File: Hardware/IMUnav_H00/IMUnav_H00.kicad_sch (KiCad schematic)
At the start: 13 parts, among them U11 OLED_I2C, U7 STM32G474VETx

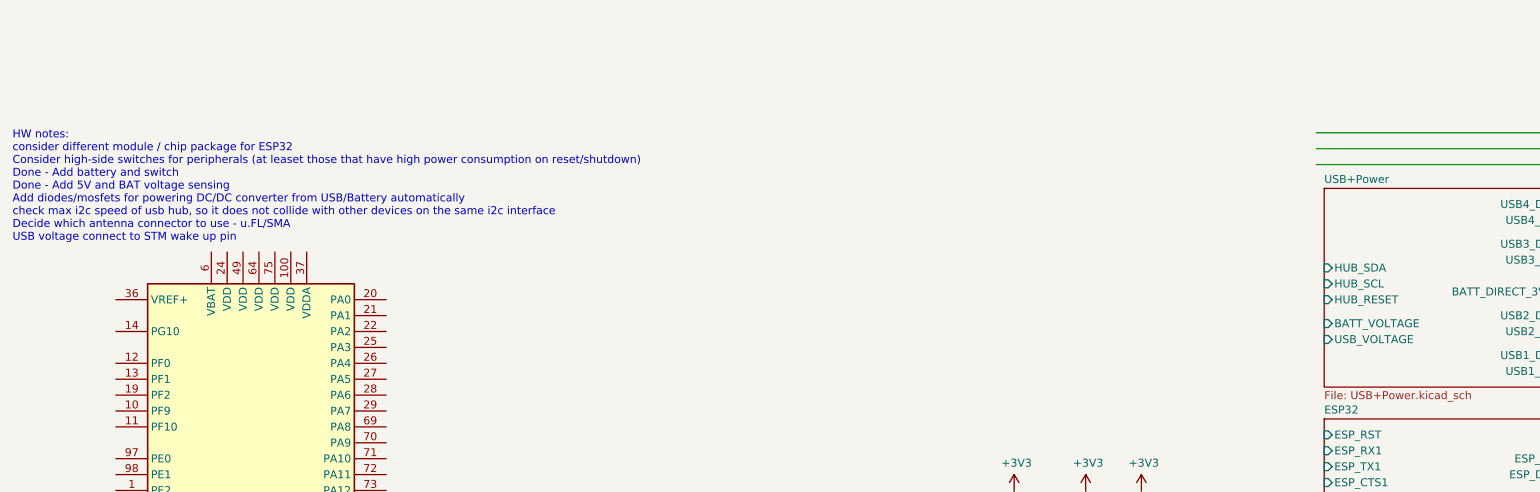
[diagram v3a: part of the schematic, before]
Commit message: Changes in power management
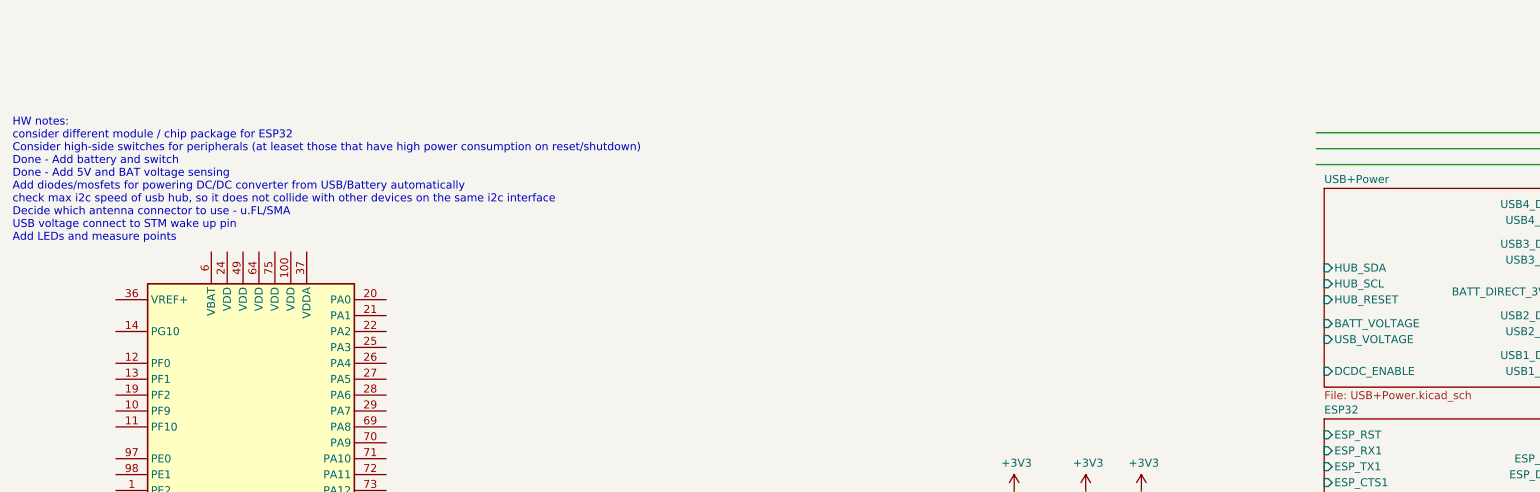
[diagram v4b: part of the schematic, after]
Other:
- sheet USB+Power ports: added DCDC_ENABLE; removed none
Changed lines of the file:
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@@
     (stroke (width 0) (type default))
   )
-  (text "HW notes:\nconsider different module / chip package for ESP32\nConsider high-side switches for peripherals (at leaset those that have high power consumption on reset/shutdown)\nDone - Add battery and switch\nDone - Add 5V and BAT voltage sensing\nAdd diodes/mosfets for powering DC/DC converter from USB/Battery automatically\ncheck max i2c speed of usb hub, so it does not collide with other devices on the same i2c interface\nDecide which antenna connector to use - u.FL/SMA\nUSB voltage connect to STM wake up pin\n\n\n"
+  (text "HW notes:\nconsider different module / chip package for ESP32\nConsider high-side switches for peripherals (at leaset those that have high power consumption on reset/shutdown)\nDone - Add battery and switch\nDone - Add 5V and BAT voltage sensing\nAdd diodes/mosfets for powering DC/DC converter from USB/Battery automatically\ncheck max i2c speed of usb hub, so it does not collide with other devices on the same i2c interface\nDecide which antenna connector to use - u.FL/SMA\nUSB voltage connect to STM wake up pin\nAdd LEDs and measure points\n\n\n"
     (at 15.24 34.29 0)
     (effects (font (size 1.27 1.27)) (justify left bottom))
@@
       (effects (font (size 1.27 1.27)) (justify right))
     )
-    (instances
+    (pin "DCDC_ENABLE" input (at 224.79 50.8 180)
+      (effects (font (size 1.27 1.27)) (justify left))
+    )
+    (instances

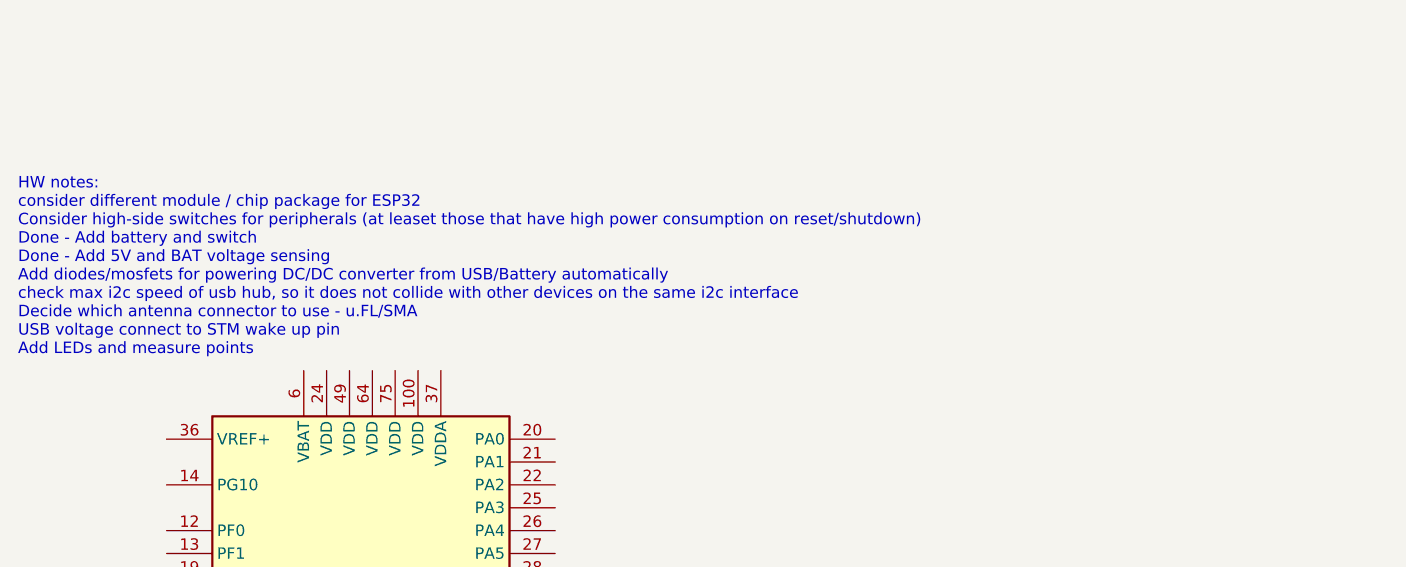
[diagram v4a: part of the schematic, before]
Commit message: Added .gitignore for KiCad file structure
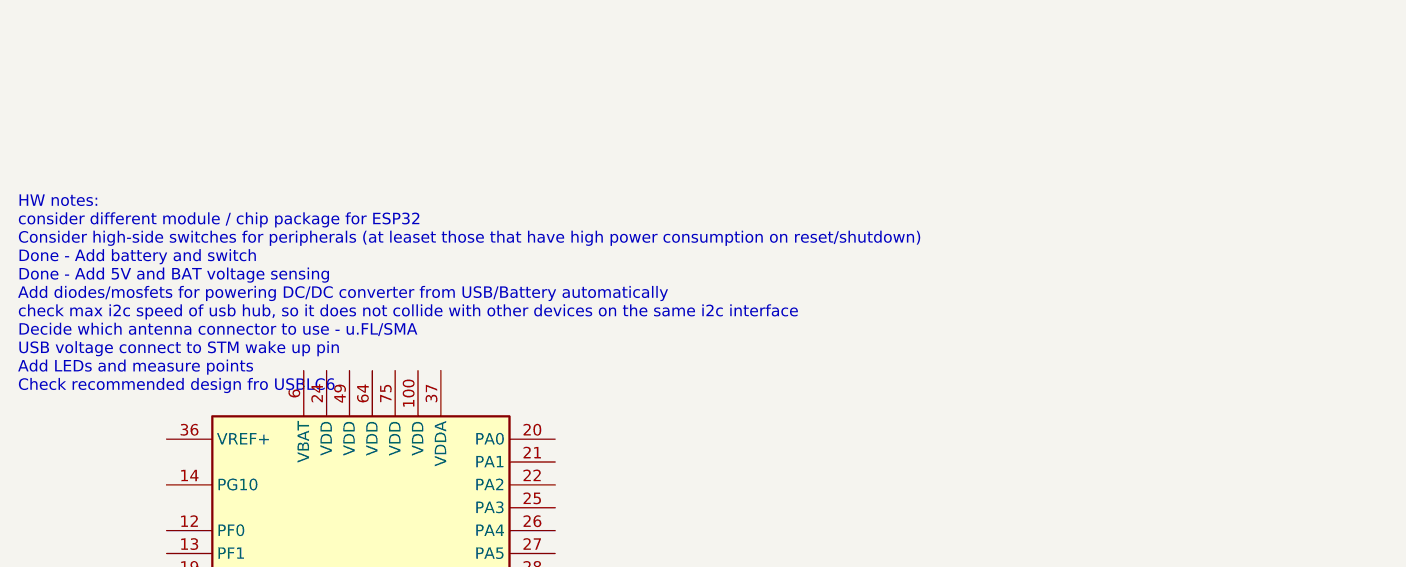
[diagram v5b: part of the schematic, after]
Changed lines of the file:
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@@
     (stroke (width 0) (type default))
   )
-  (text "HW notes:\nconsider different module / chip package for ESP32\nConsider high-side switches for peripherals (at leaset those that have high power consumption on reset/shutdown)\nDone - Add battery and switch\nDone - Add 5V and BAT voltage sensing\nAdd diodes/mosfets for powering DC/DC converter from USB/Battery automatically\ncheck max i2c speed of usb hub, so it does not collide with other devices on the same i2c interface\nDecide which antenna connector to use - u.FL/SMA\nUSB voltage connect to STM wake up pin\nAdd LEDs and measure points\n\n\n"
+  (text "HW notes:\nconsider different module / chip package for ESP32\nConsider high-side switches for peripherals (at leaset those that have high power consumption on reset/shutdown)\nDone - Add battery and switch\nDone - Add 5V and BAT voltage sensing\nAdd diodes/mosfets for powering DC/DC converter from USB/Battery automatically\ncheck max i2c speed of usb hub, so it does not collide with other devices on the same i2c interface\nDecide which antenna connector to use - u.FL/SMA\nUSB voltage connect to STM wake up pin\nAdd LEDs and measure points\nCheck recommended design fro USBLC6\n"
     (at 15.24 34.29 0)
     (effects (font (size 1.27 1.27)) (justify left bottom))

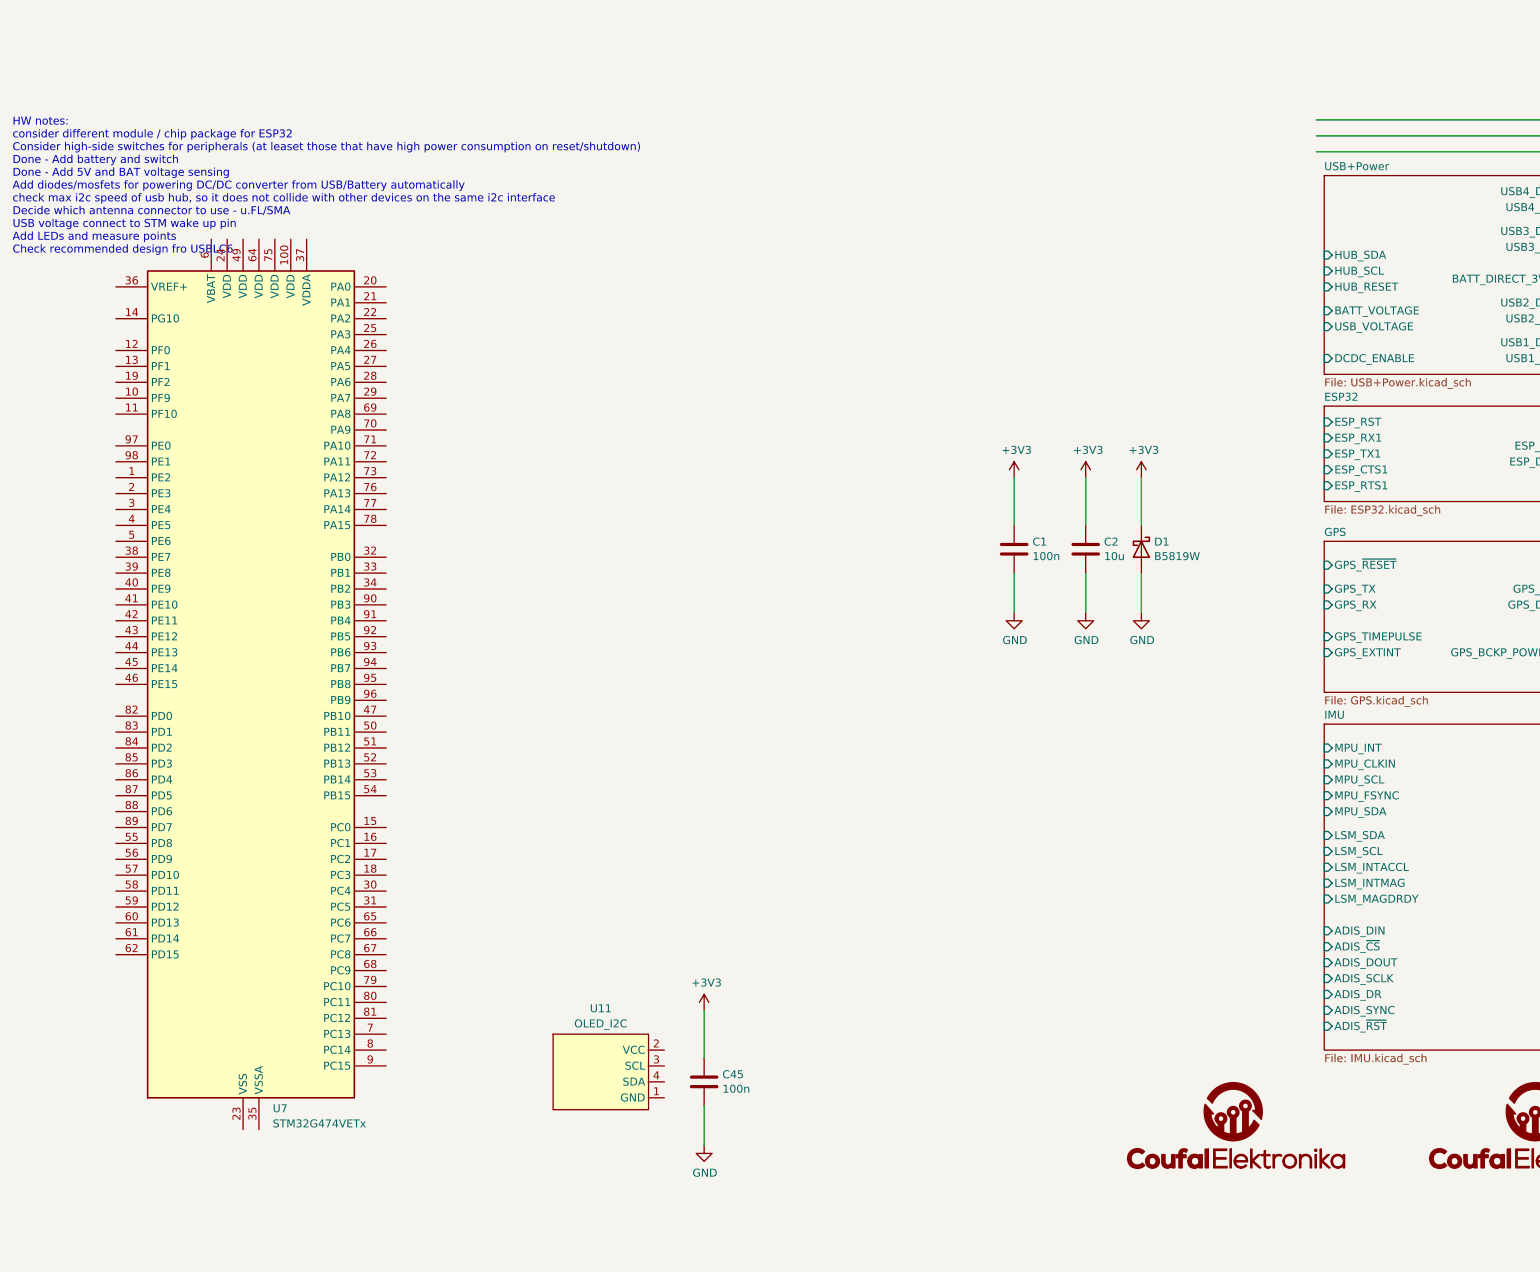
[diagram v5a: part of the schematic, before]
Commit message: Finalized and cleaned Power Management, added GPS antenna footprint
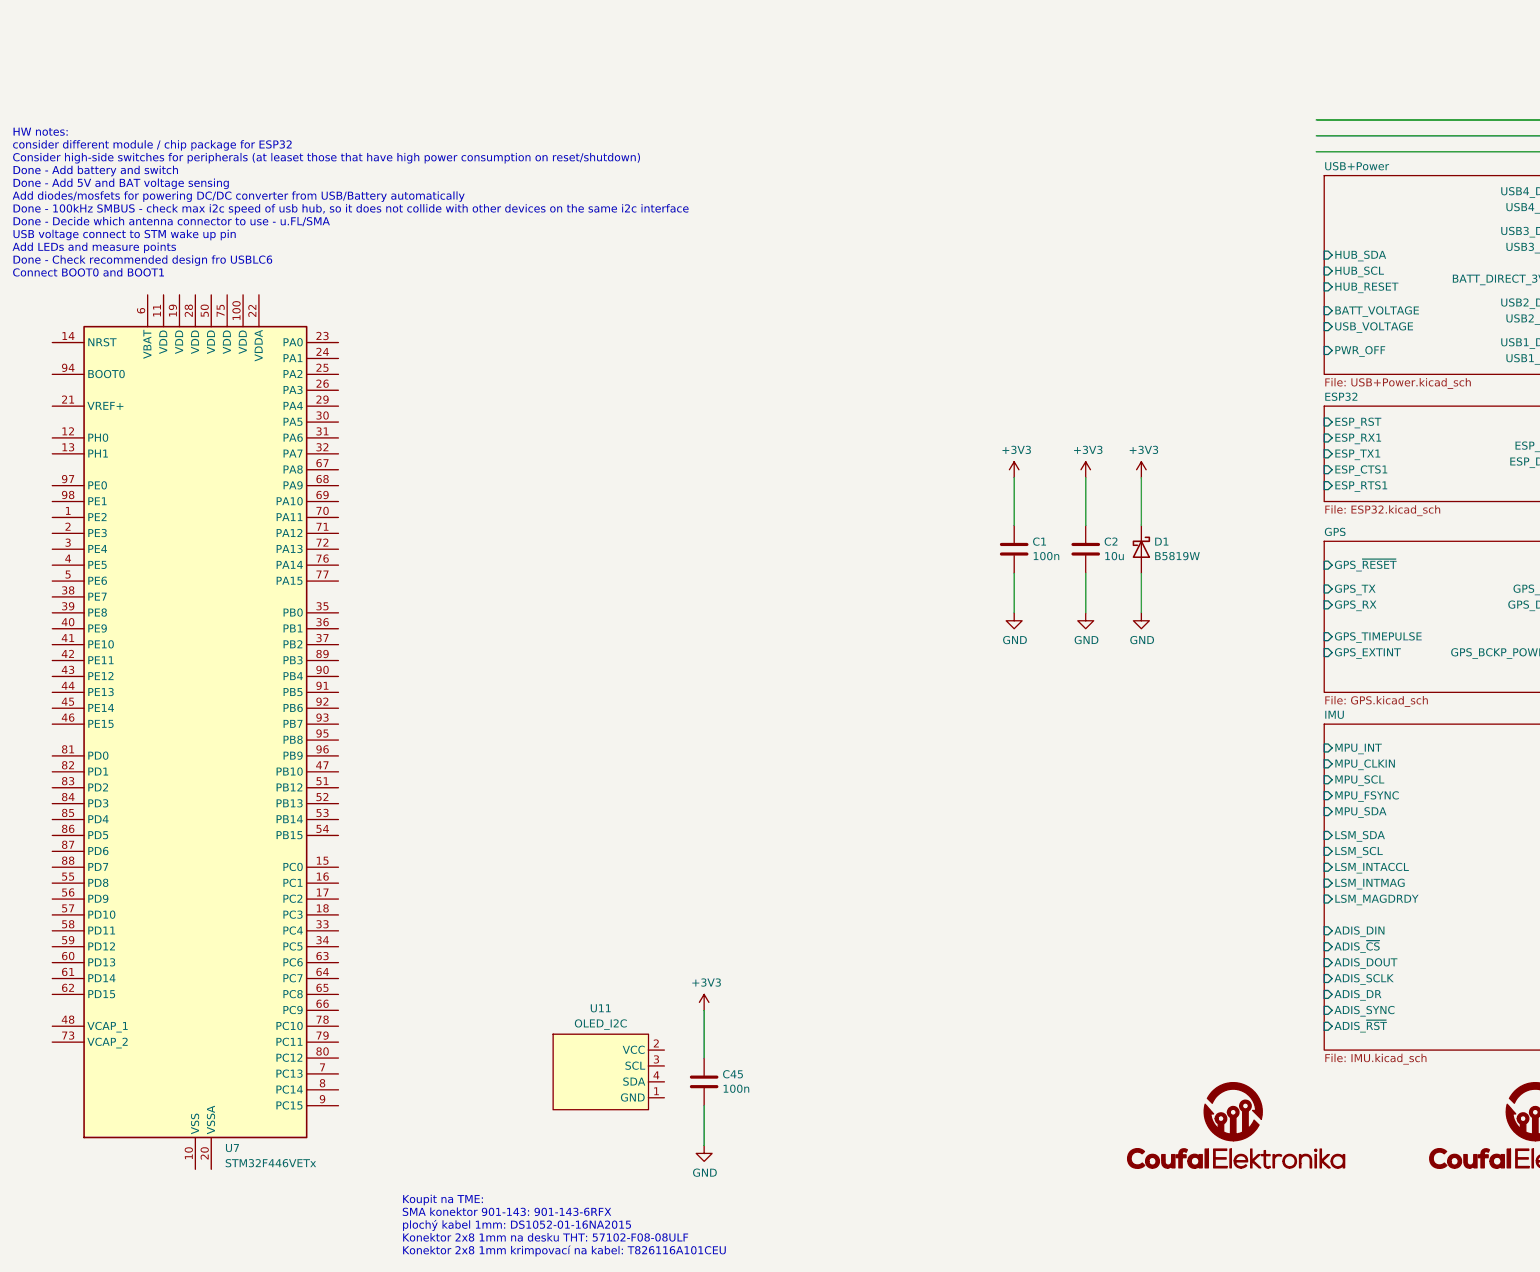
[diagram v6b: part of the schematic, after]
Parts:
- removed U7: STM32G474VETx, Package_QFP:LQFP-100_14x14mm_P0.5mm, symbol MCU_ST_STM32G4:STM32G474VETx
- added U7: STM32F446VETx, Package_QFP:LQFP-100_14x14mm_P0.5mm, symbol MCU_ST_STM32F4:STM32F446VETx
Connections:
- new net: U7.10 (VSS), U7.27 (VSS), U7.49 (VSS), U7.74 (VSS), U7.99 (VSS)
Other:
- sheet USB+Power ports: added PWR_OFF; removed DCDC_ENABLE
- note added: "HW notes: consider different module / chip package for ESP32 Consider high-side switches for peripherals (at leaset those that have high power consumption on reset/shutdown) Done - Add battery and switch Done - Add 5V and BAT voltage sensing Add diodes/mosfets for powering DC/DC converter from USB/Battery automatically Done - 100kHz SMBUS - check max i2c speed of usb hub, so it does not collide w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"
- note added: "Koupit na TME: SMA konektor 901-143: 901-143-6RFX plochý kabel 1mm: DS1052-01-16NA2015 Konektor 2x8 1mm na desku THT: 57102-F08-08ULF Konektor 2x8 1mm krimpovací na kabel: T826116A101CEU"
- note removed: "HW notes: consider different module / chip package for ESP32 Consider high-side switches for peripherals (at leaset those that have high power consumption on reset/shutdown) Done - Add battery and switch Done - Add 5V and BAT voltage sensing Add diodes/mosfets for powering DC/DC converter from USB/Battery automatically check max i2c speed of usb hub, so it does not collide with other devices on t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"
